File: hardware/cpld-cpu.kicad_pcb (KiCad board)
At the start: 4 copper layers, 264.2 x 193 mm, 392 parts, among them J1 Acc, J10 Page, J11 PC_H, J12 Conn_02x14_Odd_Even, J13 Page, J14 Conn_02x17_Odd_Even, J2 X, J3 IR, J4 AXM, J5 Dec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

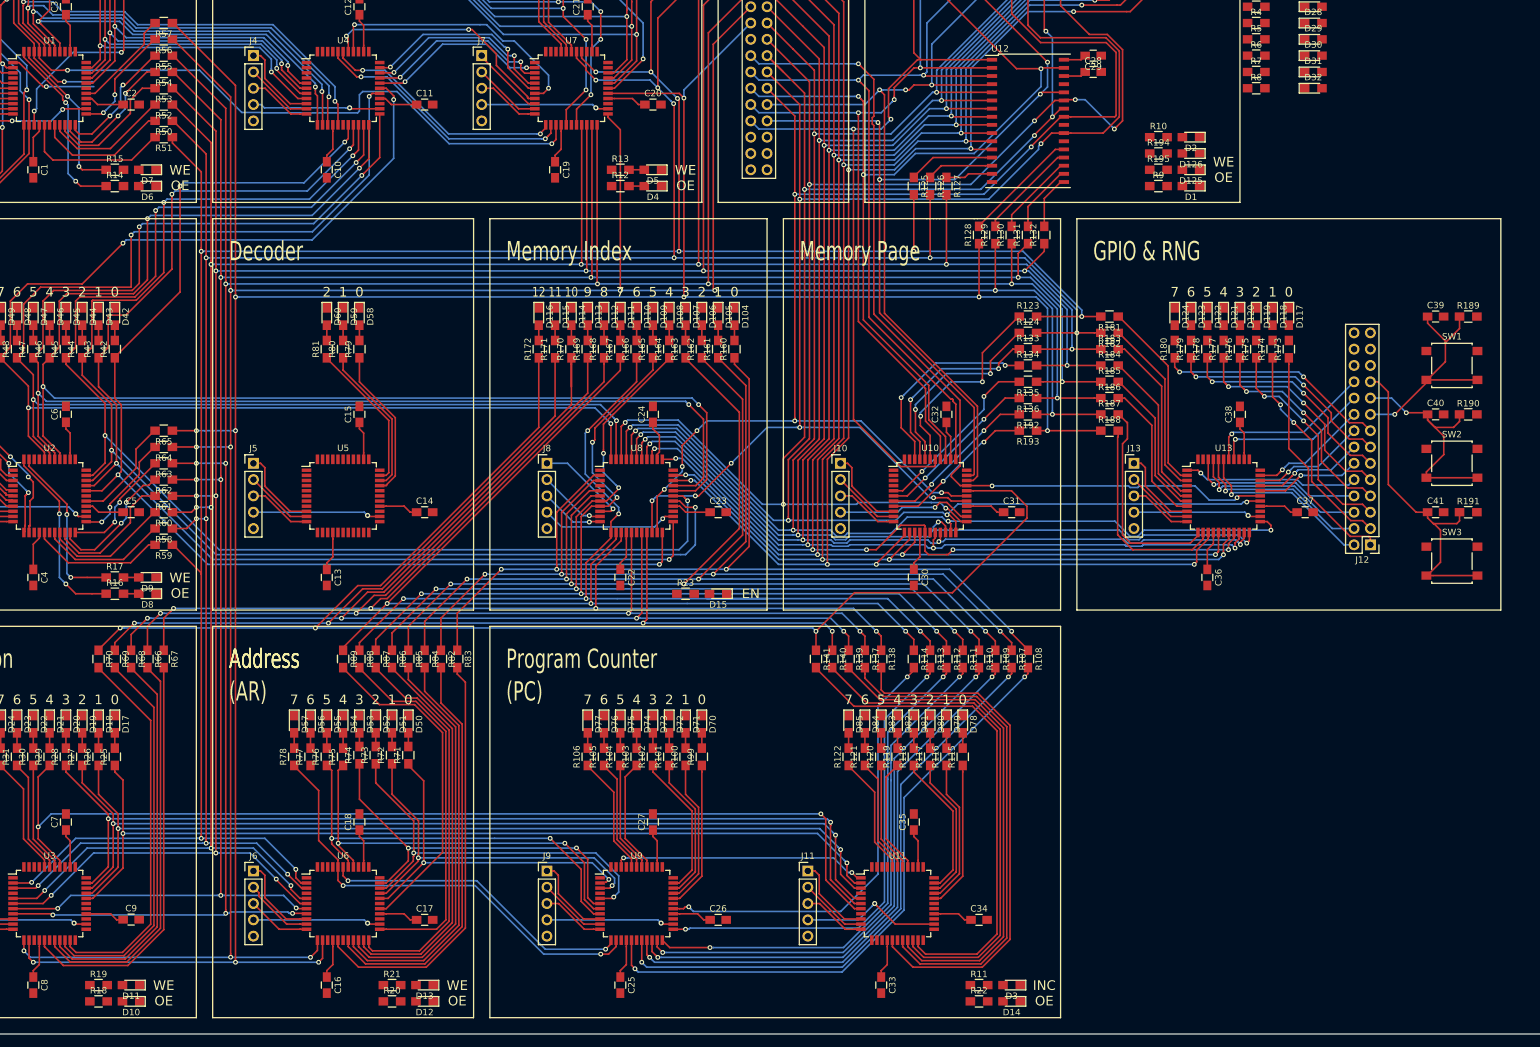
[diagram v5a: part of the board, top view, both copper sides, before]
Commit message: Clock routing
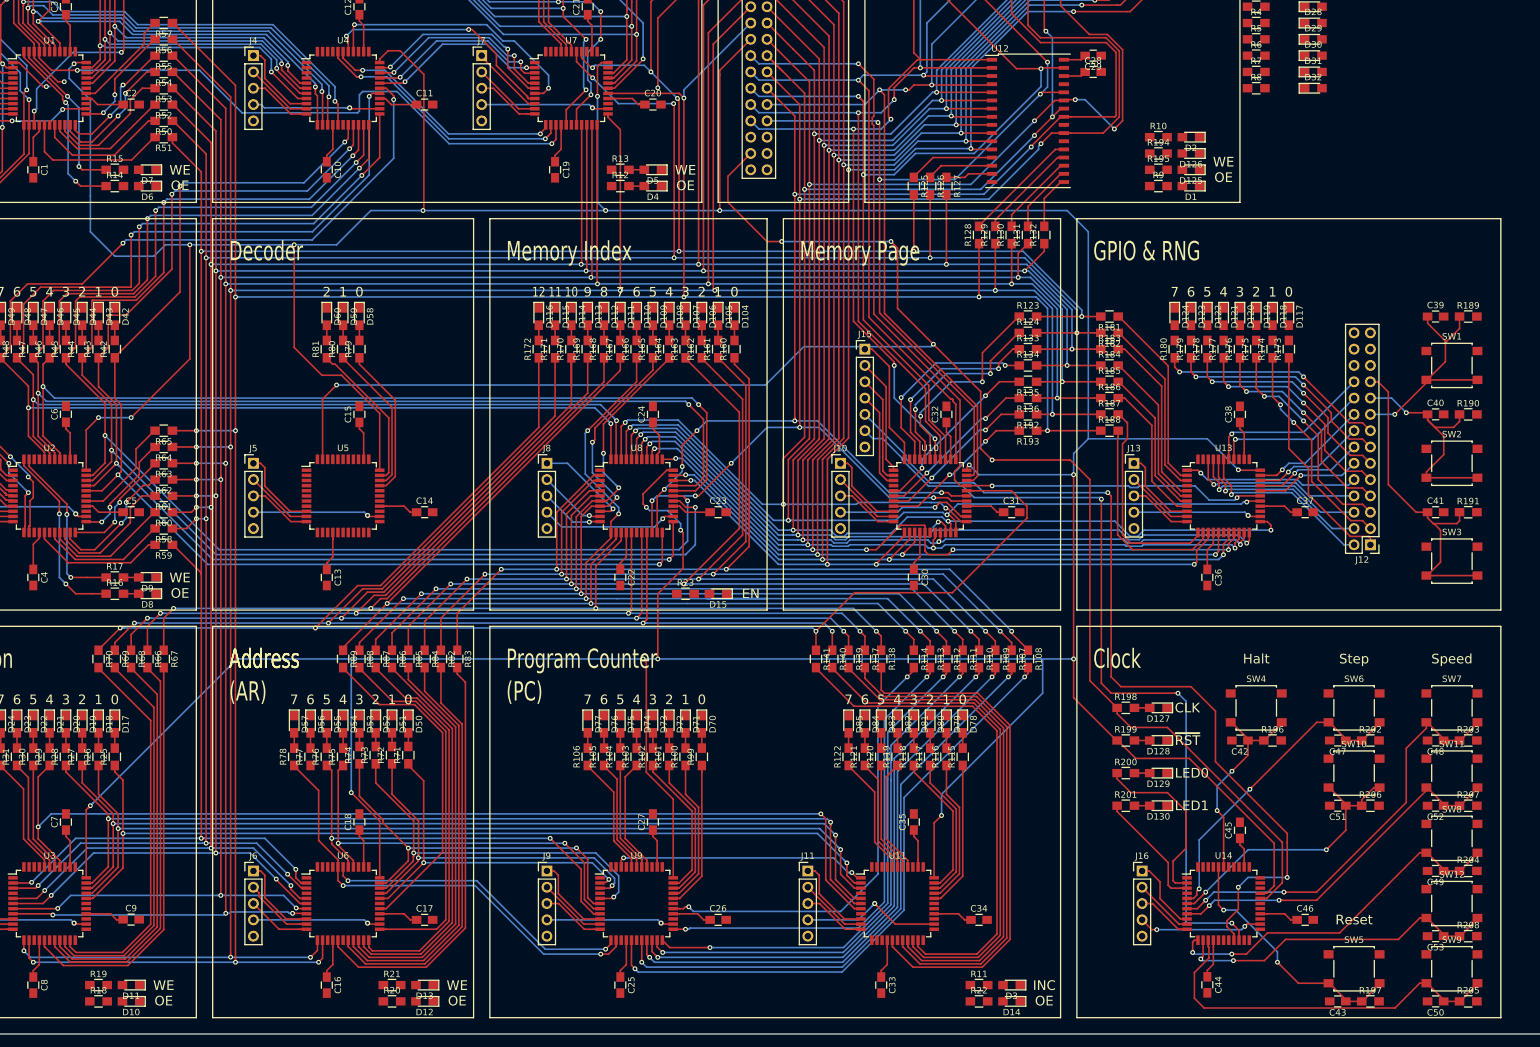
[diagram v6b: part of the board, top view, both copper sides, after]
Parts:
- added C42: 100n, Capacitors_SMD:C_0805_HandSoldering, F.Cu at (223.5, 160.0)
- added C43: 100n, Capacitors_SMD:C_0805_HandSoldering, F.Cu at (238.8, 200.7)
- added C44: 100n, Capacitors_SMD:C_0805_HandSoldering, F.Cu at (218.4, 198.1)
- added C45: 100n, Capacitors_SMD:C_0805_HandSoldering, F.Cu at (223.5, 174.0)
- added C46: 100n, Capacitors_SMD:C_0805_HandSoldering, F.Cu at (233.7, 188.0)
- added C47: 100n, Capacitors_SMD:C_0805_HandSoldering, F.Cu at (238.8, 160.0)
- added C48: 100n, Capacitors_SMD:C_0805_HandSoldering, F.Cu at (254.0, 160.0)
- added C49: 100n, Capacitors_SMD:C_0805_HandSoldering, F.Cu at (254.0, 180.3)
- added C50: 100n, Capacitors_SMD:C_0805_HandSoldering, F.Cu at (254.0, 200.7)
- added C51: 100n, Capacitors_SMD:C_0805_HandSoldering, F.Cu at (238.8, 170.2)
- added C52: 100n, Capacitors_SMD:C_0805_HandSoldering, F.Cu at (254.0, 170.2)
- added C53: 100n, Capacitors_SMD:C_0805_HandSoldering, F.Cu at (254.0, 190.5)
- added D127: LED_Small, LEDs:LED_0805_HandSoldering, F.Cu at (210.8, 154.9)
- added D128: LED_Small, LEDs:LED_0805_HandSoldering, F.Cu at (210.8, 160.0)
- added D129: LED_Small, LEDs:LED_0805_HandSoldering, F.Cu at (210.8, 165.1)
- added D130: LED_Small, LEDs:LED_0805_HandSoldering, F.Cu at (210.8, 170.2)
- added J15: Conn_01x07, Pin_Headers:Pin_Header_Straight_1x07_Pitch2.54mm, F.Cu at (165.1, 99.1)
- added J16: Clock, Pin_Headers:Pin_Header_Straight_1x05_Pitch2.54mm, F.Cu at (208.3, 180.3)
- added R196: 10k, Resistors_SMD:R_0805_HandSoldering, F.Cu at (228.6, 160.0)
- added R197: 10k, Resistors_SMD:R_0805_HandSoldering, F.Cu at (243.8, 200.7)
- added R198: 2k, Resistors_SMD:R_0805_HandSoldering, F.Cu at (205.7, 154.9)
- added R199: 2k, Resistors_SMD:R_0805_HandSoldering, F.Cu at (205.7, 160.0)
- added R200: 2k, Resistors_SMD:R_0805_HandSoldering, F.Cu at (205.7, 165.1)
- added R201: 2k, Resistors_SMD:R_0805_HandSoldering, F.Cu at (205.7, 170.2)
- added R202: 10k, Resistors_SMD:R_0805_HandSoldering, F.Cu at (243.8, 160.0)
- added R203: 10k, Resistors_SMD:R_0805_HandSoldering, F.Cu at (259.1, 160.0)
- added R204: 10k, Resistors_SMD:R_0805_HandSoldering, F.Cu at (259.1, 180.3)
- added R205: 10k, Resistors_SMD:R_0805_HandSoldering, F.Cu at (259.1, 200.7)
- added R206: 10k, Resistors_SMD:R_0805_HandSoldering, F.Cu at (243.8, 170.2)
- added R207: 10k, Resistors_SMD:R_0805_HandSoldering, F.Cu at (259.1, 170.2)
- added R208: 10k, Resistors_SMD:R_0805_HandSoldering, F.Cu at (259.1, 190.5)
- added SW10: Step 8, Buttons_Switches_SMD:SW_SPST_B3S-1000, F.Cu at (241.3, 165.1)
- added SW11: S1, Buttons_Switches_SMD:SW_SPST_B3S-1000, F.Cu at (256.5, 165.1)
- added SW12: S3, Buttons_Switches_SMD:SW_SPST_B3S-1000, F.Cu at (256.5, 185.4)
- added SW4: Halt, Buttons_Switches_SMD:SW_SPST_B3S-1000, F.Cu at (226.1, 154.9)
- added SW5: Reset, Buttons_Switches_SMD:SW_SPST_B3S-1000, F.Cu at (241.3, 195.6)
- added SW6: Step 1, Buttons_Switches_SMD:SW_SPST_B3S-1000, F.Cu at (241.3, 154.9)
- added SW7: S0, Buttons_Switches_SMD:SW_SPST_B3S-1000, F.Cu at (256.5, 154.9)
- added SW8: S2, Buttons_Switches_SMD:SW_SPST_B3S-1000, F.Cu at (256.5, 175.3)
- added SW9: S4, Buttons_Switches_SMD:SW_SPST_B3S-1000, F.Cu at (256.5, 195.6)
- added U14: Clock, Housings_QFP:TQFP-44_10x10mm_Pitch0.8mm, F.Cu at (221.0, 185.4)
- J13: value Page -> GPIO
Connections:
- U10 pad 1: Net-(U10-Pad1) -> /PROG1
- U10 pad 2: Net-(U10-Pad2) -> /PROG2
- U10 pad 3: Net-(U10-Pad3) -> /PROG3
- U10 pad 44: Net-(U10-Pad44) -> /PROG0
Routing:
- net /RST: track 0.00 -> 857.8 mm, vias 0 -> 20
- net /CLK: track 0.00 -> 285.2 mm, vias 0 -> 5
- net /PROG4: track 0.00 -> 138.8 mm, vias 0 -> 3
- net /PROG5: track 0.00 -> 129.6 mm, vias 0 -> 3
- net /BTN_S0: track 0.00 -> 65.3 mm, vias 0 -> 2
- net /BTN_S4: track 0.00 -> 58.9 mm
- net /BTN_S1: track 0.00 -> 56.2 mm, vias 0 -> 2
- net /BTN_S2: track 0.00 -> 56.2 mm, vias 0 -> 2
- net /BTN_S3: track 0.00 -> 51.6 mm, vias 0 -> 2
- net /BTN_STEP1: track 0.00 -> 48.8 mm, vias 0 -> 2
- net /BTN_STEP8: track 0.00 -> 44.3 mm, vias 0 -> 2
- net /BTN_RST: track 0.00 -> 39.6 mm, vias 0 -> 2
- net /BTN_HALT: track 0.00 -> 32.6 mm, vias 0 -> 2
- net /LED0: track 0.00 -> 27.7 mm
- net /PROG0: track 0.00 -> 20.4 mm
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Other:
- board text added: "CLK"
- board text added: "Clock"
- board text added: "Halt"
- board text added: "LED0"
- board text added: "LED1"
- board text added: "Reset"
- board text added: "Speed"
- board text added: "Step"
- board text added: "~RST~"

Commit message: Finished ratsnest
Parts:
- added D131: LED_Small, LEDs:LED_0805_HandSoldering, F.Cu at (53.3, 68.6)
- added R209: 2k, Resistors_SMD:R_0805_HandSoldering, F.Cu at (48.3, 68.6)
- moved D25 19.2 mm to (215.9, 43.2), turned to 180 degrees
- moved D26 19.2 mm to (215.9, 45.7), turned to 180 degrees
- moved D27 19.2 mm to (215.9, 48.3), turned to 180 degrees
- moved D28 19.2 mm to (215.9, 50.8), turned to 180 degrees
- moved D29 19.2 mm to (215.9, 53.3), turned to 180 degrees
- moved D30 19.2 mm to (215.9, 55.9), turned to 180 degrees
- moved D31 19.2 mm to (215.9, 58.4), turned to 180 degrees
- moved D32 19.2 mm to (215.9, 61.0), turned to 180 degrees
- moved R5 15.5 mm to (210.8, 53.3)
- moved R1 15.5 mm to (210.8, 43.2)
- moved R2 15.5 mm to (210.8, 45.7)
- moved R3 15.5 mm to (210.8, 48.3)
- moved R4 15.5 mm to (210.8, 50.8)
- moved R6 15.5 mm to (210.8, 55.9)
- moved R7 15.5 mm to (210.8, 58.4)
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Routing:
- net GND: track 0.00 -> 594.2 mm, vias 0 -> 244
- net /RAM_WE: track 0.00 -> 296.3 mm, vias 0 -> 11
- net /GPIO_OE: track 0.00 -> 208.9 mm, vias 0 -> 4
- net /IR5: track 17.2 -> 205.0 mm, vias 0 -> 8
- net /PC_OE: track 0.00 -> 167.9 mm, vias 0 -> 6
- net /IR7: track 18.6 -> 182.7 mm, vias 0 -> 6
- net /PC_INC: track 0.00 -> 151.9 mm, vias 0 -> 4
- net /PC_WE: track 0.00 -> 136.6 mm, vias 0 -> 4
- net /IR_OE: track 0.00 -> 128.2 mm, vias 0 -> 4
- net /DEV_OE: track 0.00 -> 122.5 mm, vias 0 -> 2
- net /ALU_OE: track 0.00 -> 121.5 mm, vias 0 -> 5
- net /ALU_WE: track 0.00 -> 120.0 mm, vias 0 -> 5
- net /IR_WE: track 0.00 -> 119.4 mm, vias 0 -> 4
- net /A_CC: track 7.27 -> 124.0 mm, vias 1 -> 4
- net /A_Z: track 34.4 -> 146.3 mm, vias 1 -> 4
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- added copper zone on In1.Cu, net GND
- added copper zone on In2.Cu, net VCC
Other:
- board size 264.2 x 193 mm -> 259.1 x 198.1 mm
- board text added: "13"
- board text added: "14"
- board text added: "15"
- board text added: "16"
- board text added: "17"
- board text added: "CC WE OE"
- board text added: "Data"
- board text added: "EXPN"
- board text added: "GPIO"
- board text added: "RAM"
- board text added: "WE OE OE OE"
